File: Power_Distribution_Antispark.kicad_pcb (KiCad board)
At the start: 4 copper layers, 61.5 x 76 mm, 131 parts, among them J1 STM Signal Conn, J10 CSense12V_2 Conn, J11 CSense12V_3 Conn, J2 +48V Battery Conn, J3 Motor Conn, J4 CSense3V3STM Conn, J5 CSense3V3_2 Conn, J6 CSense5V_1 Conn, J7 CSense5V_2 Conn, J8 CSense5V_3 Conn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

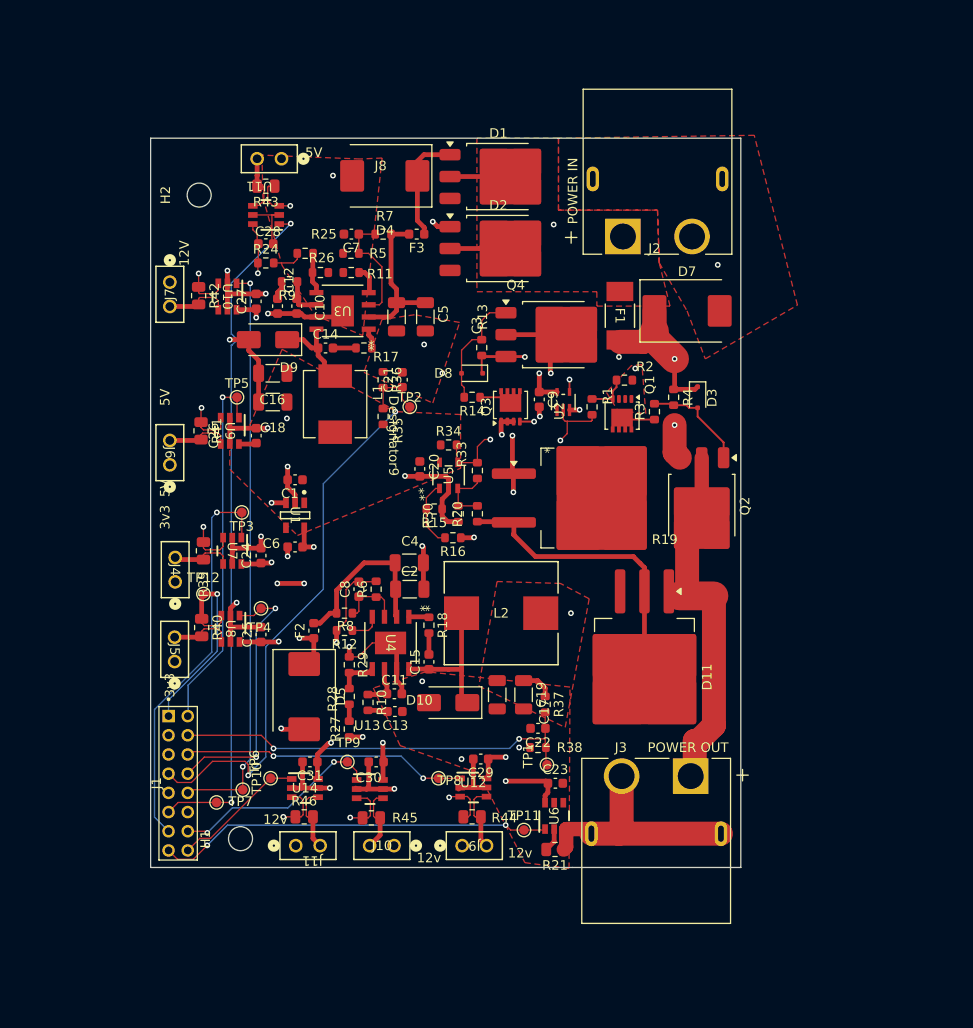
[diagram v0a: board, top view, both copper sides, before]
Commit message: layout review + fixed polygon pour shapes
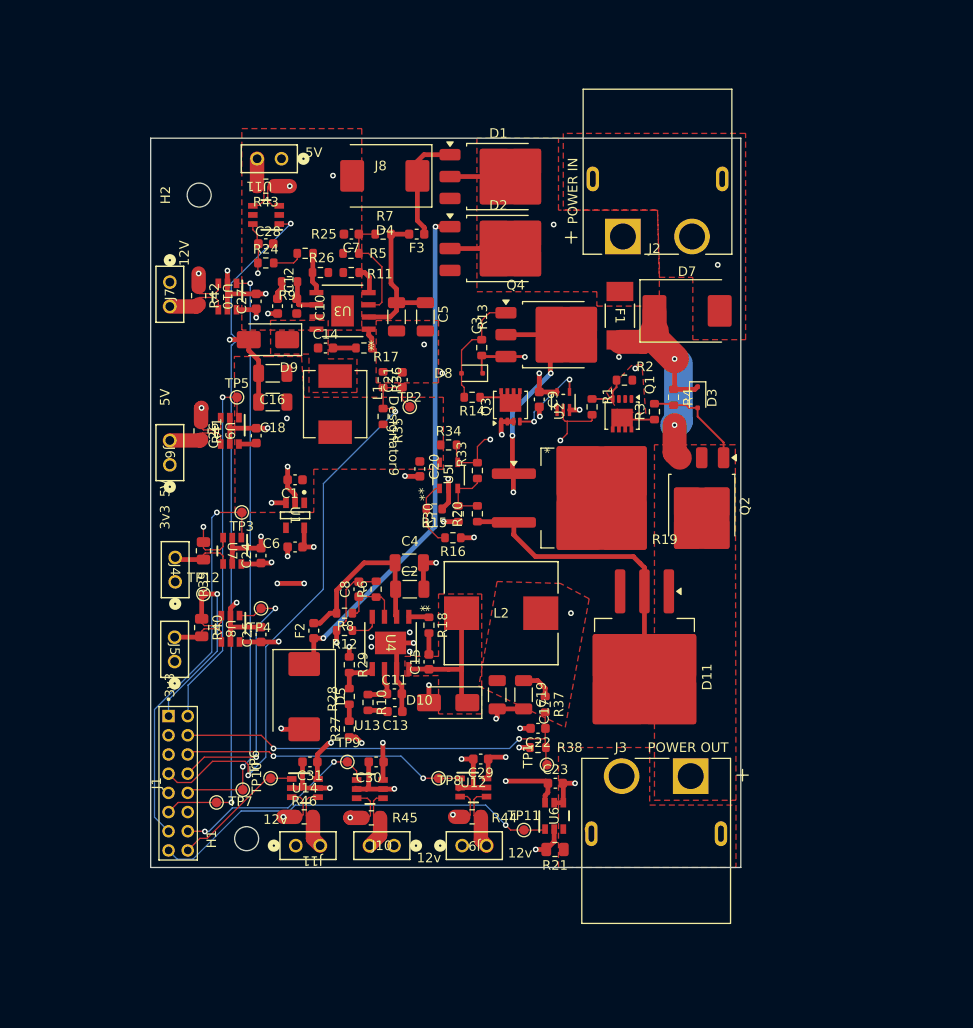
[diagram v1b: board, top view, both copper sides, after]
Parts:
- moved H1 0.63 mm to (170.0, 122.0)
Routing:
- net /MotorConn: track 37.3 -> 3.02 mm
- net Net-(J3-N): track 24.7 -> 0.75 mm
- net Net-(D9-K): track 9.28 -> 0.25 mm
- net GND: track 124.9 -> 121.4 mm, vias 26 -> 37
- net Net-(D2-K): track 55.8 -> 53.4 mm
- net /PreCharge_Sense: track 41.3 -> 43.1 mm, vias 2 -> 1
- added copper zone on F.Cu, net /MotorConn
- added copper zone on F.Cu, net Net-(D10-K)
- added copper zone on F.Cu, net Net-(D9-K)
- added copper zone on F.Cu, net Net-(J3-N)

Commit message: layout update
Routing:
- net +12V: track 19.8 -> 16.3 mm, vias 5 -> 21
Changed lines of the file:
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@@
 	)
 	(segment
-		(start 202.950852 116.225001)
-		(end 204.225001 116.225001)
-		(width 0.5)
-		(layer "F.Cu")
-		(net 1)
-	)
-	(segment
 		(start 168.314998 98.75085)
 		(end 168.314998 97.985002)
@@
 	)
 	(segment
+		(start 202.925851 116.2)
+		(end 204.2 116.2)
+		(width 0.5)
+		(layer "F.Cu")
+		(net 1)
+	)
+	(segment
 		(start 200.5 77)
 		(end 200.5 78)
@@
 	)
 	(via
-		(at 174.274999 92.574999)
+		(at 204.2 116.2)
 		(size 0.6)
 		(drill 0.3)
@@
 	)
 	(via
-		(at 210.5 73)
+		(at 174.274999 92.574999)
 		(size 0.6)
 		(drill 0.3)
 		(layers "F.Cu" "B.Cu")
-		(free yes)
 		(net 1)
 	)
 	(via
-		(at 187 102.5)
+		(at 210.5 73)
 		(size 0.6)
 		(drill 0.3)
 		(layers "F.Cu" "B.Cu")
+		(free yes)
 		(net 1)
 	)
 	(via
-		(at 186.5 84.2)
+		(at 187 102.5)
 		(size 0.6)
 		(drill 0.3)
@@
 	)
 	(via
-		(at 171.5 90.5)
+		(at 186.5 84.2)
 		(size 0.6)
 		(drill 0.3)
@@
 	)
 	(via
-		(at 204.225001 116.225001)
+		(at 171.5 90.5)
 		(size 0.6)
 		(drill 0.3)
@@
 	)
 	(via
-		(at 187 100.5)
-		(size 0.6)
-		(drill 0.3)
-		(layers "F.Cu" "B.Cu")
-		(net 1)
-	)
-	(via
 		(at 172.225 67.275)
 		(size 0.6)
@@
 	)
 	(via
+		(at 187 100.5)
+		(size 0.6)
+		(drill 0.3)
+		(layers "F.Cu" "B.Cu")
+		(free yes)
+		(net 1)
+	)
+	(via
 		(at 192.4 113.7)
 		(size 0.6)
@@
 	)
 	(segment
-		(start 171.225 60)
-		(end 171.225 61.95)
-		(width 0.127)
-		(layer "F.Cu")
-		(net 2)
-	)
-	(segment
 		(start 177.375 115.697499)
 		(end 177.4525 115.774999)
@@
 	)
 	(segment
+		(start 171.225 60)
+		(end 171.225 63.025)
+		(width 0.5)
+		(layer "F.Cu")
+		(net 2)
+	)
+	(segment
 		(start 166.700004 65.2)
 		(end 167.050002 64.850002)
@@
 	)
 	(segment
+		(start 171.225 63.025)
+		(end 171.175 63.075)
+		(width 0.5)
+		(layer "F.Cu")
+		(net 2)
+	)
+	(segment
 		(start 165.25 79.15)
 		(end 165.5 79.4)
@@
 	)
 	(segment
-		(start 171.175 62)
-		(end 171.175 63.075)
-		(width 0.127)
-		(layer "F.Cu")
-		(net 2)
-	)
-	(segment
 		(start 170.900001 80.874999)
 		(end 171 80.775)
@@
 	)
 	(segment
-		(start 198.865 105.52585)
-		(end 200.32585 105.52585)
-		(width 0.5)
-		(layer "F.Cu")
-		(net 16)
-	)
-	(segment
 		(start 193.3 119.525)
 		(end 193.3 117.9)
@@
 	)
 	(segment
-		(start 200.32585 105.52585)
-		(end 201.115 106.315)
-		(width 0.5)
-		(layer "F.Cu")
-		(net 16)
-	)
-	(segment
-		(start 201.115 106.315)
-		(end 201.115 107.17585)
-		(width 0.5)
-		(layer "F.Cu")
-		(net 16)
-	)
-	(segment
 		(start 192.269498 117.6)
 		(end 192.25 117.619498)
@@
 	)
 	(via
+		(at 203.6 103.1)
+		(size 0.6)
+		(drill 0.3)
+		(layers "F.Cu" "B.Cu")
+		(free yes)
+		(net 16)
+	)
+	(via
+		(at 201.5 103.3)
+		(size 0.6)
+		(drill 0.3)
+		(layers "F.Cu" "B.Cu")
+		(free yes)
+		(net 16)
+	)
+	(via
+		(at 196.8 102.7)
+		(size 0.6)
+		(drill 0.3)
+		(layers "F.Cu" "B.Cu")
+		(free yes)
+		(net 16)
+	)
+	(via
+		(at 203.5 105.3)
+		(size 0.6)
+		(drill 0.3)
+		(layers "F.Cu" "B.Cu")
+		(free yes)
+		(net 16)
+	)
+	(via
+		(at 203.7 101)
+		(size 0.6)
+		(drill 0.3)
+		(layers "F.Cu" "B.Cu")
+		(free yes)
+		(net 16)
+	)
+	(via
+		(at 201.4 105.3)
+		(size 0.6)
+		(drill 0.3)
+		(layers "F.Cu" "B.Cu")
+		(free yes)
+		(net 16)
+	)
+	(via
+		(at 196.9 98.6)
+		(size 0.6)
+		(drill 0.3)
+		(layers "F.Cu" "B.Cu")
+		(free yes)
+		(net 16)
+	)
+	(via
 		(at 180.8 119.8)
 		(size 0.6)
@@
 	)
 	(via
+		(at 201.6 101.4)
+		(size 0.6)
+		(drill 0.3)
+		(layers "F.Cu" "B.Cu")
+		(free yes)
+		(net 16)
+	)
+	(via
+		(at 203.6 107.1)
+		(size 0.6)
+		(drill 0.3)
+		(layers "F.Cu" "B.Cu")
+		(free yes)
+		(net 16)
+	)
+	(via
+		(at 195.9 97.4)
+		(size 0.6)
+		(drill 0.3)
+		(layers "F.Cu" "B.Cu")
+		(free yes)
+		(net 16)
+	)
+	(via
+		(at 195.7 99.8)
+		(size 0.6)
+		(drill 0.3)
+		(layers "F.Cu" "B.Cu")
+		(free yes)
+		(net 16)
+	)
+	(via
+		(at 197.9 99.8)
+		(size 0.6)
+		(drill 0.3)
+		(layers "F.Cu" "B.Cu")
+		(free yes)
+		(net 16)
+	)
+	(via
 		(at 191.5 119.5)
 		(size 0.6)
@@
 	)
 	(via
+		(at 198 101.5)
+		(size 0.6)
+		(drill 0.3)
+		(layers "F.Cu" "B.Cu")
+		(free yes)
+		(net 16)
+	)
+	(via
+		(at 197.8 97.4)
+		(size 0.6)
+		(drill 0.3)
+		(layers "F.Cu" "B.Cu")
+		(free yes)
+		(net 16)
+	)
+	(via
 		(at 173.825 119.725)
 		(size 0.6)
@@
 		(net 16)
 	)
+	(via
+		(at 195.7 101.6)
+		(size 0.6)
+		(drill 0.3)
+		(layers "F.Cu" "B.Cu")
+		(free yes)
+		(net 16)
+	)
+	(via
+		(at 199.8 102.5)
+		(size 0.6)
+		(drill 0.3)
+		(layers "F.Cu" "B.Cu")
+		(free yes)
+		(net 16)
+	)
 	(segment
 		(start 169.833824 113.9355)
@@
 	)
 	(zone
-		(net 1)
-		(net_name "GND")
+		(net 16)
+		(net_name "+12V")
 		(layer "F.Cu")
 		(hatch edge 0.5)
-		(priority 7)
+		(priority 10)
 		(connect_pads yes
 			(clearance 0.5)
@@
 		(polygon
 			(pts
-				(xy 210.1 72.7) (xy 207.5 75.5) (xy 208.7 77.4) (xy 211.6 77.715) (xy 211.2 72.6)
+				(xy 194.8 96.3) (xy 205.1 96.3) (xy 205 108.3) (xy 194.8 108.3)
 			)
 		)
@@
 		(layer "F.Cu")
 		(hatch edge 0.5)
-		(priority 8)
+		(priority 7)
 		(connect_pads yes
 			(clearance 0.5)
@@
 		(polygon
 			(pts
-				(xy 190 68) (xy 190 74.5) (xy 183.5 74.5) (xy 183.5 68)
+				(xy 210.1 72.7) (xy 207.5 75.5) (xy 208.7 77.4) (xy 211.6 77.715) (xy 211.2 72.6)
 			)
 		)
 	)
 	(zone
-		(net 16)
-		(net_name "+12V")
+		(net 1)
+		(net_name "GND")
 		(layer "F.Cu")
 		(hatch edge 0.5)
-		(priority 10)
+		(priority 8)
 		(connect_pads yes
 			(clearance 0.5)
@@
 		(polygon
 			(pts
-				(xy 202.7 95.4) (xy 196.1 95.2) (xy 194.2 106.1) (xy 203.2 110.4) (xy 205.7 97)
+				(xy 190 68) (xy 190 74.5) (xy 183.5 74.5) (xy 183.5 68)
 			)
 		)
@@
 		(polygon
 			(pts
-				(xy 178 89) (xy 158 85) (xy 159 104.5) (xy 173 104.5) (xy 183 88)
+				(xy 177 88) (xy 158.012435 85.242487) (xy 159 104.5) (xy 173 104.5) (xy 183 88)
 			)
 		)

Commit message: layout post review
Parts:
- moved R21 3.09 mm to (203.6, 120.4), turned to 90 degrees
- moved TP11 2.13 mm to (197.5, 119.5)
- moved U6 1.56 mm to (200.5, 119.5)
- moved C23 1.56 mm to (200.6, 116.1)
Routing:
- net GND: track 121.4 -> 123.5 mm, vias 37 -> 43
- net +5V: track 122.0 -> 120.9 mm, vias 15 -> 30
- net Net-(J3-N): track 0.75 -> 0.68 mm, vias 0 -> 19
- net /MotorConn: vias 0 -> 37
- added copper zone on B.Cu, net /MotorConn
- added copper zone on In2.Cu, net /MotorConn
- added copper zone on B.Cu, net Net-(J3-N)
- added copper zone on In2.Cu, net Net-(J3-N)

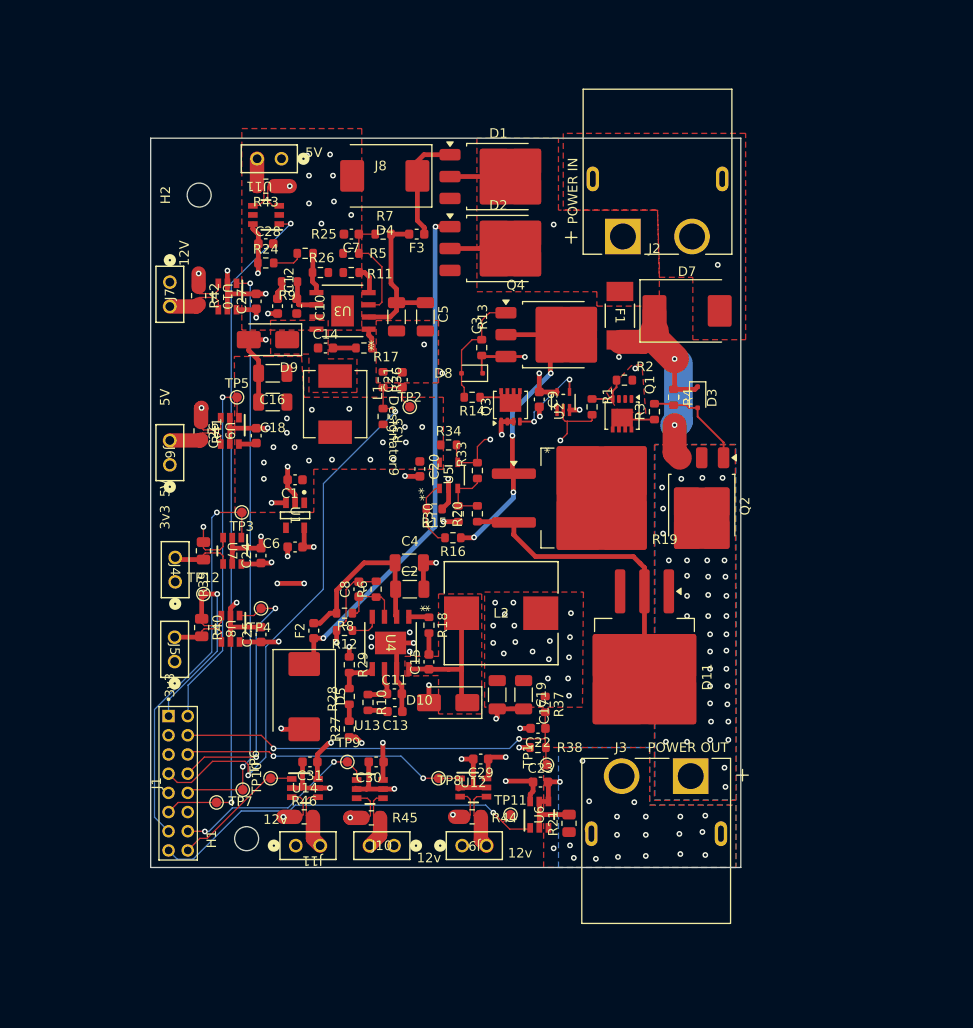
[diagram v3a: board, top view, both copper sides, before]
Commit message: fixed silkscreens
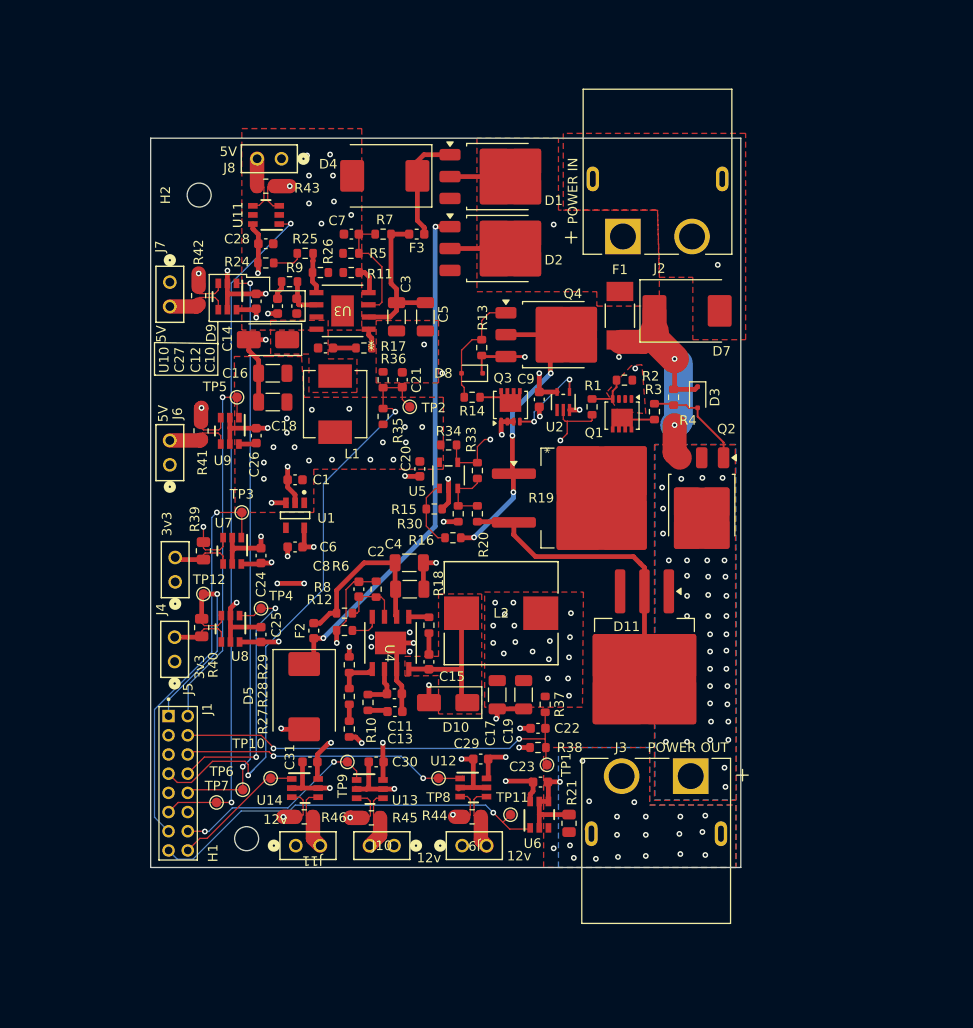
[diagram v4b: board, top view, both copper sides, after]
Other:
- board text removed: "12V"

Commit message: fixed connectors
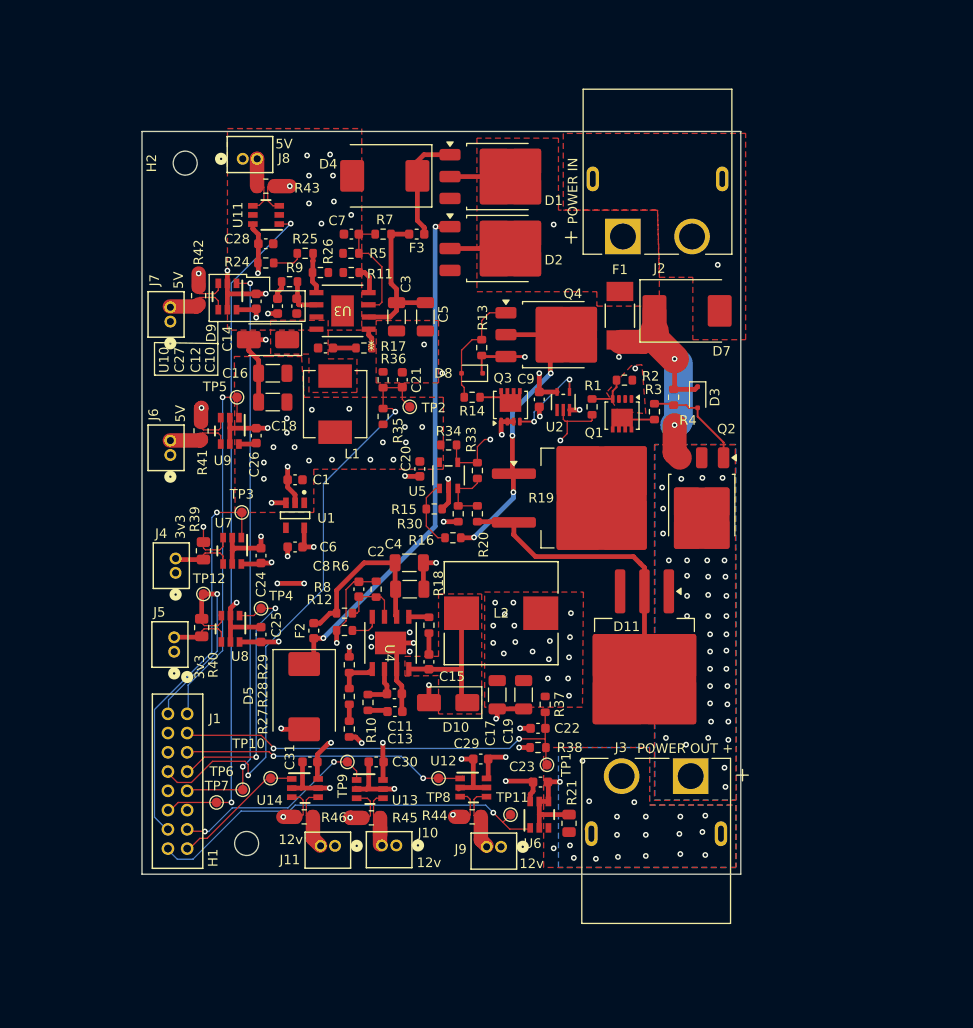
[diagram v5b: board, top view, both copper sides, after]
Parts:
- D11: value PNU650150AEJJ -> PNU650200AEJJ
- J1: footprint CustomFootprintLibrary:ADAM_2PH2-16-UA -> CustomFootprintLibrary:CONN16_B16B-PHDSS_JST
- J10, J11, J4, J5, J6, J7, J8, J9: footprint CustomFootprintLibrary:M20-9990246 -> CustomFootprintLibrary:CONN_B2B-ZR_02P_JST
- R10, R9: value 13K -> 13.3K
- moved J1 7.30 mm to (163.8, 109.0)
- moved J7 4.12 mm to (162.1, 68.1)
- moved J11 4.09 mm to (179.2, 122.7)
- moved J9 4.06 mm to (196.5, 122.8)
- moved J8 4.04 mm to (169.6, 51.2)
- moved H2 3.63 mm to (163.6, 51.6)
- moved J6 1.02 mm to (162.1, 82.0), turned to 90 degrees
- moved J5 1.02 mm to (162.5, 102.5), turned to 90 degrees
- moved J4 0.94 mm to (162.6, 94.3), turned to 90 degrees
- moved H1 0.50 mm to (170.0, 122.5)
- moved J10 0.24 mm to (185.6, 122.7), turned to 180 degrees
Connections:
- J1 pad 1: +3V3 -> /C_Sense_5V_1
- J1 pad 10: /C_Sense_5V_2 -> GND
- J1 pad 11: /C_Sense_5V_3 -> GND
- J1 pad 12: GND -> /C_Sense_5V_3
- J1 pad 13: /C_Sense_3V3_STM -> /C_Sense_12V_2
- J1 pad 14: /C_Sense_12V_2 -> /C_Sense_3V3_STM
- J1 pad 15: /PreCharge_Sense -> /C_Sense_12V_3
- J1 pad 16: /C_Sense_12V_3 -> /PreCharge_Sense
- J1 pad 2: /C_Sense_5V_1 -> +3V3
- J1 pad 3: GND -> /V_S_12V_Output
- J1 pad 4: /V_S_12V_Output -> GND
- J1 pad 5: GND -> /C_Sense_12V_1
- J1 pad 6: /C_Sense_12V_1 -> GND
- J1 pad 7: /V_S_5V_Output -> /C_Sense_3V3
- J1 pad 8: /C_Sense_3V3 -> /V_S_5V_Output
- J1 pad 9: GND -> /C_Sense_5V_2
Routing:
- net /V_S_5V_Output: track 63.9 -> 63.1 mm
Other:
- board size 61.5 x 76 mm -> 62.4 x 77.4 mm
- board text added: "POWER OUT +"
- board text removed: "POWER OUT"

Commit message: fixed leo layout review
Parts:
- moved J11 0.72 mm to (178.5, 122.7)
- moved J9 0.62 mm to (195.9, 122.8)
- moved H1 0.30 mm to (169.7, 122.5)
- moved J7 0.22 mm to (162.1, 67.9)
- moved TP7 0.12 mm to (166.9, 118.1)
- moved J10 0.08 mm to (185.5, 122.7)
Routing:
- net Net-(D10-K): track 15.1 -> 2.96 mm
- net Net-(U13-IN-): track 7.06 -> 6.36 mm
- net +12V: track 16.3 -> 16.6 mm, vias 21 -> 19
- net Net-(J3-N): vias 19 -> 18
- net GND: vias 43 -> 48
- net +5V: vias 30 -> 29
- net +48V: vias 1 -> 8
- added copper zone on B.Cu, net +48V
- added copper zone on B.Cu, net GND

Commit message: final layout + logo added
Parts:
- added G***: LOGO, CustomFootprintLibrary:LBH, B.Cu at (182.4, 61.0)
- added G***: LOGO, CustomFootprintLibrary:ElectriumLogo20, B.Cu at (190.2, 54.0)
- moved TP11 1.00 mm to (196.7, 120.1)
- moved R21 0.91 mm to (203.5, 119.5)
- moved C23 0.53 mm to (200.1, 116.1)
- moved U6 0.40 mm to (200.1, 119.5)
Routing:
- net GND: track 123.5 -> 111.3 mm, vias 48 -> 60
- net Net-(J3-N): track 0.68 -> 4.71 mm
- net /PreCharge_Sense: track 42.8 -> 41.1 mm
- net +5V: track 120.9 -> 120.0 mm
- net /MotorConn: vias 37 -> 39
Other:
- board text added: "Eleanor Wang"
- board text added: "Power Distribution AntiSpark"

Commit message: added date and rev number
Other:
- board text added: "6/21/2026"
- board text added: "Rev 1.0"
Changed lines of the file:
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@@
+		)
+	)
+	(gr_text "6/21/2026"
+		(at 200.9 58.6 0)
+		(layer "B.SilkS")
+		(effects
+			(font
+				(size 1 1)
+				(thickness 0.15)
+			)
+			(justify left bottom mirror)
 		)
 	)
@@
 		(layer "B.SilkS")
 		(effects
+			(font
+				(size 1 1)
+				(thickness 0.15)
+			)
+			(justify left bottom mirror)
+		)
+	)
+	(gr_text "Rev 1.0"
+		(at 200.9475 57 0)
+		(layer "B.SilkS")
+		(effects
